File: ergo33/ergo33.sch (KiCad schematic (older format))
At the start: 113 parts, among them SW1 SW_Push, SW46 Rotary_Encoder_Switch, U1 ATmega32U4-AU, Y1 16MHz

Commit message: Start trace layout
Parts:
- removed F2: 500mA, Fuse:Fuse_1206_3216Metric, symbol Device:Polyfuse_Small
- added JP4: SolderJumper_2_Open, Jumper:SolderJumper-2_P1.3mm_Open_Pad1.0x1.5mm, symbol Jumper:SolderJumper_2_Open
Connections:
- net at USB2.5 (VBUS): now also JP4.1 (A)
- net PWR_IN: now reaches F1.1, USB1.16 (VBUS), USB1.21 (VBUS), USB1.4 (VBUS), USB1.9 (VBUS)
- net PWR_IN: now also JP4.2 (B)
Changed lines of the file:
@@
 	4400 6350 5000 6350
 Wire Wire Line
-	1650 6150 1900 6150
+	1650 6150 1850 6150
 Connection ~ 1650 6150
 $Comp
@@
 Text GLabel 2100 6450 2    50   Input ~ 0
 D-
-Wire Wire Line
-	2100 6150 2250 6150
-$Comp
-L Device:Polyfuse_Small F2
-U 1 1 5F2186AC
-P 2000 6150
-F 0 "F2" V 1795 6150 50  0000 C CNN
-F 1 "500mA" V 1886 6150 50  0000 C CNN
-F 2 "Fuse:Fuse_1206_3216Metric" H 2050 5950 50  0001 L CNN
-F 3 "~" H 2000 6150 50  0001 C CNN
-	1    2000 6150
-	0    1    1    0
-$EndComp
-$Comp
-L power:+5V #PWR0116
-U 1 1 5F210B55
-P 2250 6150
-F 0 "#PWR0116" H 2250 6000 50  0001 C CNN
-F 1 "+5V" H 2265 6323 50  0000 C CNN
-F 2 "" H 2250 6150 50  0001 C CNN
-F 3 "" H 2250 6150 50  0001 C CNN
-	1    2250 6150
-	1    0    0    -1
-$EndComp
 Connection ~ 1350 6550
 Wire Wire Line
@@
 Wire Wire Line
 	10900 5950 10950 5950
+$Comp
+L Jumper:SolderJumper_2_Open JP4
+U 1 1 5F1CFCA6
+P 2000 6150
+F 0 "JP4" H 2000 6355 50  0000 C CNN
+F 1 "SolderJumper_2_Open" H 2000 6264 50  0000 C CNN
+F 2 "Jumper:SolderJumper-2_P1.3mm_Open_Pad1.0x1.5mm" H 2000 6150 50  0001 C CNN
+F 3 "~" H 2000 6150 50  0001 C CNN
+	1    2000 6150
+	1    0    0    -1
+$EndComp
+Wire Wire Line
+	2150 6150 2250 6150
+Text GLabel 2250 6150 2    50   Input ~ 0
+PWR_IN
+Text GLabel 4850 5850 3    50   Input ~ 0
+PWR_IN
 $EndSCHEMATC

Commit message: Rerouting ergo33
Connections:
- net ROW0: now also U1.41 (PF0)
- net ROW1: now also U1.40 (PF1)
- net ROW2: now also U1.39 (PF4)
- net ROW3: now also U1.38 (PF5)
- net ROW4: now also U1.37 (PF6)
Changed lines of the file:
@@
 Text GLabel 4850 5850 3    50   Input ~ 0
 PWR_IN
+Text GLabel 3150 4100 2    50   Input ~ 0
+ROW0
+Text GLabel 3150 4200 2    50   Input ~ 0
+ROW1
+Text GLabel 3150 4300 2    50   Input ~ 0
+ROW2
+Text GLabel 3150 4400 2    50   Input ~ 0
+ROW3
+Text GLabel 3150 4500 2    50   Input ~ 0
+ROW4
 $EndSCHEMATC

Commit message: Finish ergo33 routing v1
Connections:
- net COL0: now also U1.32 (PC7)
- net COL1: now also U1.31 (PC6)
- net COL2: now also U1.30 (PB6)
- net COL3: now also U1.29 (PB5)
- net COL4: now also U1.28 (PB4)
- net COL5: now also U1.27 (PD7)
- net COL6: now also U1.26 (PD6)
- net LEDS: now also JP1.2 (C), U1.25 (PD4); no longer JP1.1 (A)
- net at LED1.4 (DIN): now also JP1.1 (A); no longer JP1.2 (C)
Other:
- moved on the sheet: JP1, R4
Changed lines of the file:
@@
 L Device:R_Small R4
 U 1 1 5F14E7F9
-P 3350 3800
-F 0 "R4" V 3154 3800 50  0000 C CNN
-F 1 "10k" V 3245 3800 50  0000 C CNN
-F 2 "Resistor_SMD:R_0805_2012Metric" H 3350 3800 50  0001 C CNN
-F 3 "~" H 3350 3800 50  0001 C CNN
-	1    3350 3800
+P 3450 3800
+F 0 "R4" V 3254 3800 50  0000 C CNN
+F 1 "10k" V 3345 3800 50  0000 C CNN
+F 2 "Resistor_SMD:R_0805_2012Metric" H 3450 3800 50  0001 C CNN
+F 3 "~" H 3450 3800 50  0001 C CNN
+	1    3450 3800
 	0    1    1    0
 $EndComp
@@
 	1    0    0    -1
 $EndComp
-Wire Wire Line
-	3150 3800 3250 3800
-Wire Wire Line
-	3450 3800 3600 3800
 $Comp
 L Device:R_Small R3
@@
 	1    0    0    -1
 $EndComp
-Text GLabel 5400 4450 0    50   Input ~ 0
+Text GLabel 5750 4450 2    50   Input ~ 0
 LEDS
 Wire Wire Line
@@
 	1300 2000 1200 2000
 Wire Wire Line
-	5600 4600 5600 4850
-Wire Wire Line
 	10800 6050 10800 5700
 Connection ~ 10800 6050
 Wire Wire Line
 	10800 6050 10950 6050
-Text GLabel 5800 4450 2    50   Input ~ 0
+Text GLabel 5600 4250 1    50   Input ~ 0
 LEDS2
 Wire Wire Line
@@
 F 3 "~" H 5600 4450 50  0001 C CNN
 	1    5600 4450
-	1    0    0    -1
+	0    -1   -1   0
 $EndComp
 Wire Wire Line
@@
 Text GLabel 3150 4500 2    50   Input ~ 0
 ROW4
+Wire Wire Line
+	5600 4650 5600 4850
+Text GLabel 3150 2700 2    50   Input ~ 0
+COL0
+Text GLabel 3150 2600 2    50   Input ~ 0
+COL1
+Text GLabel 3150 2300 2    50   Input ~ 0
+COL2
+Text GLabel 3150 2200 2    50   Input ~ 0
+COL3
+Text GLabel 3150 2100 2    50   Input ~ 0
+COL4
+Text GLabel 3150 3600 2    50   Input ~ 0
+COL5
+Wire Wire Line
+	3550 3800 3600 3800
+Wire Wire Line
+	3150 3800 3350 3800
+Text GLabel 3150 3500 2    50   Input ~ 0
+COL6
+Text GLabel 3150 3300 2    50   Input ~ 0
+LEDS
 $EndSCHEMATC

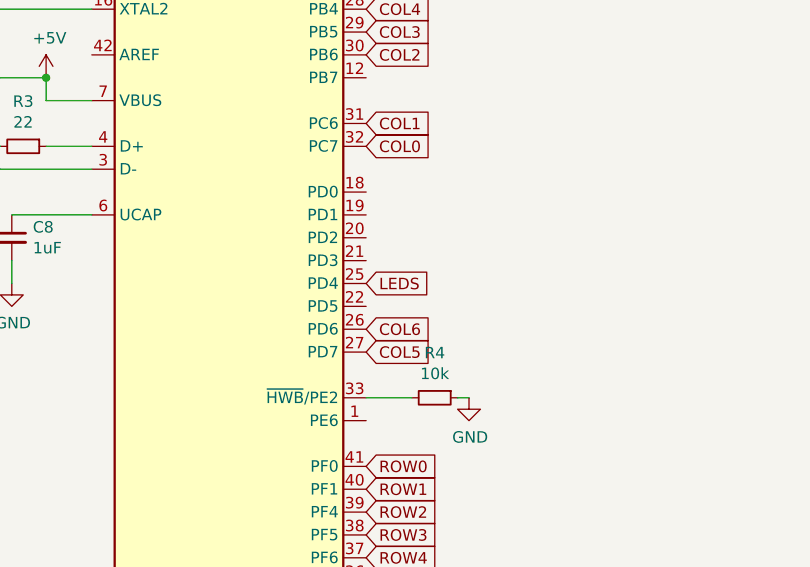
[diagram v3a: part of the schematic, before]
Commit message: Fix ergo33 routing
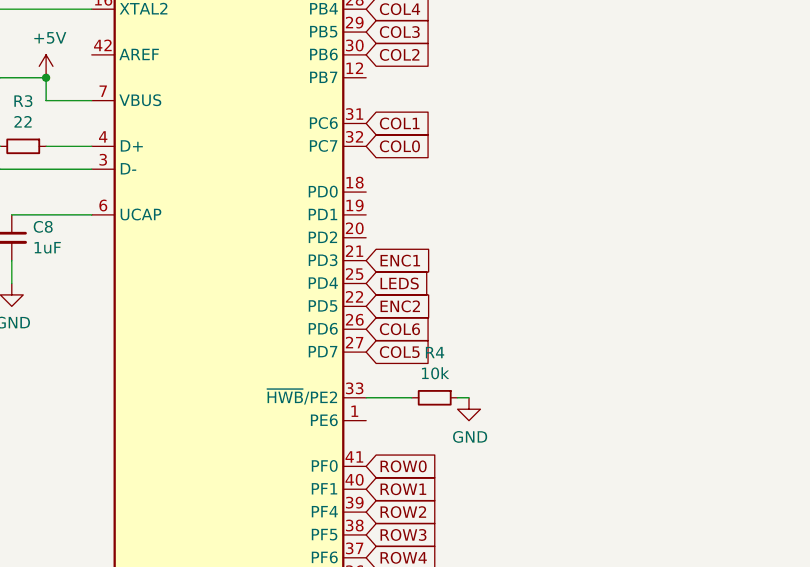
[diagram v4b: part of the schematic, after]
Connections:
- net ENC1: now also U1.21 (PD3)
- net ENC2: now also U1.22 (PD5)
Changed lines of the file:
@@
 Text GLabel 3150 3300 2    50   Input ~ 0
 LEDS
+Text GLabel 3150 3200 2    50   Input ~ 0
+ENC1
+Text GLabel 3150 3400 2    50   Input ~ 0
+ENC2
 $EndSCHEMATC

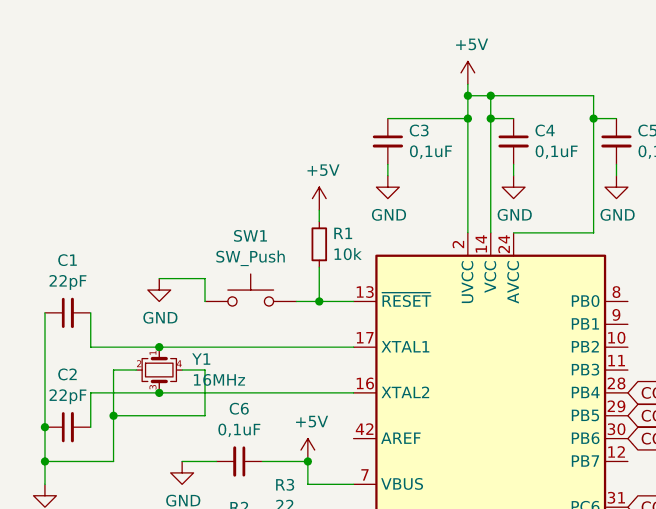
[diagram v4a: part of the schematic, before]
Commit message: Add arc suppression cap to ergo33
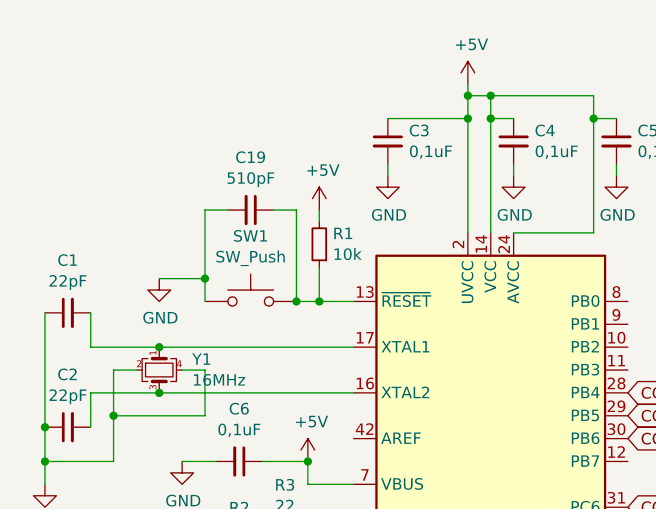
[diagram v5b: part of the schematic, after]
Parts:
- added C19: 510pF, Capacitor_SMD:C_0805_2012Metric, symbol Device:C_Small
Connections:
- net GND: now also C19.2
- net at R1.1, SW1.2, U1.13 (~RESET): now also C19.1
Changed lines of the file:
@@
 Text GLabel 3150 3400 2    50   Input ~ 0
 ENC2
+$Comp
+L Device:C_Small C19
+U 1 1 5F1BC5FF
+P 1500 1300
+F 0 "C19" V 1271 1300 50  0000 C CNN
+F 1 "510pF" V 1362 1300 50  0000 C CNN
+F 2 "Capacitor_SMD:C_0805_2012Metric" H 1500 1300 50  0001 C CNN
+F 3 "~" H 1500 1300 50  0001 C CNN
+	1    1500 1300
+	0    1    1    0
+$EndComp
+Wire Wire Line
+	1700 1700 1700 1300
+Wire Wire Line
+	1700 1300 1600 1300
+Connection ~ 1700 1700
+Wire Wire Line
+	1400 1300 1300 1300
+Wire Wire Line
+	1300 1300 1300 1600
+Connection ~ 1300 1600
 $EndSCHEMATC

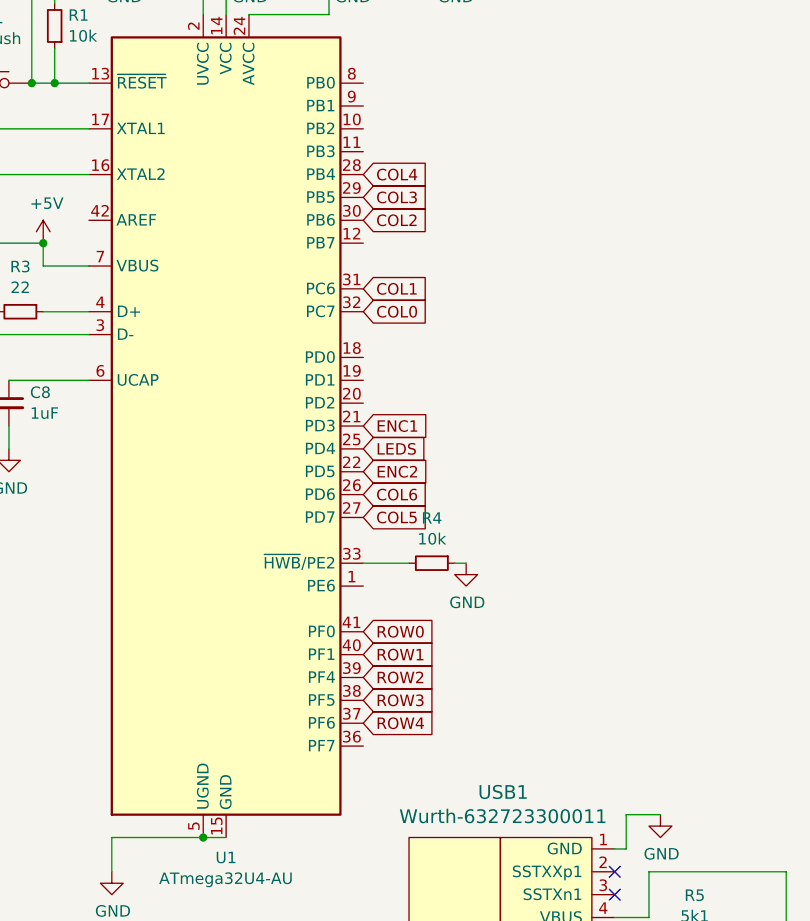
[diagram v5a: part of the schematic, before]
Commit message: Reroute ergo33 MCU area
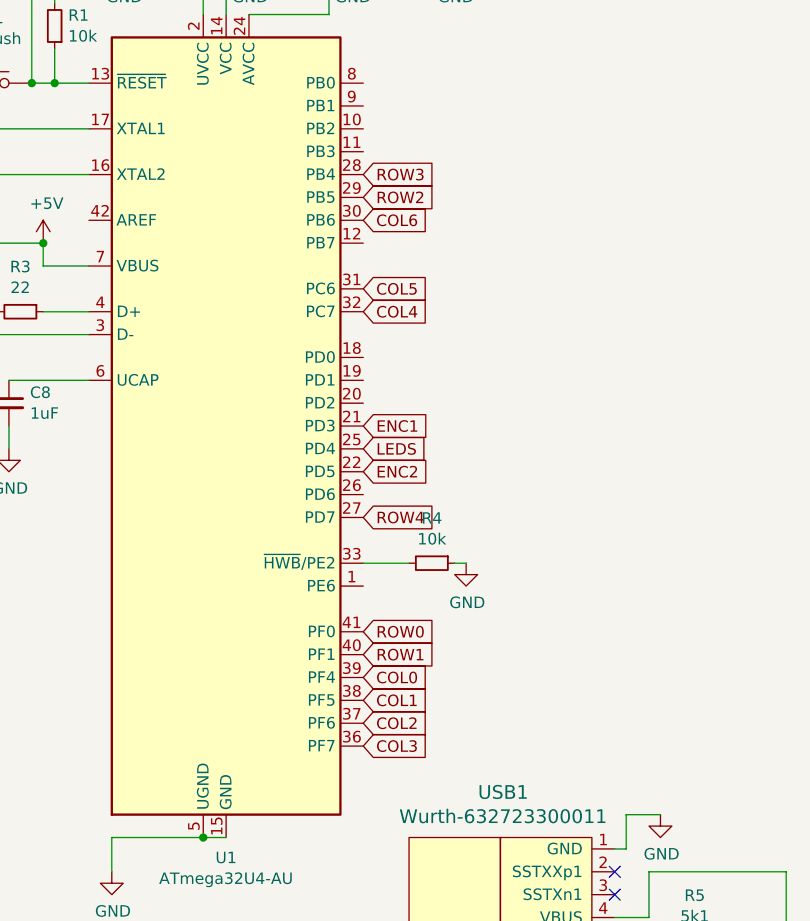
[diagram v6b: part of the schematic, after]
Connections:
- net COL0: now also U1.39 (PF4); no longer U1.32 (PC7)
- net COL1: now also U1.38 (PF5); no longer U1.31 (PC6)
- net COL2: now also U1.37 (PF6); no longer U1.30 (PB6)
- net COL3: now also U1.36 (PF7); no longer U1.29 (PB5)
- net COL4: now also U1.32 (PC7); no longer U1.28 (PB4)
- net COL5: now also U1.31 (PC6); no longer U1.27 (PD7)
- net COL6: now also U1.30 (PB6); no longer U1.26 (PD6)
- net ROW2: now also U1.29 (PB5); no longer U1.39 (PF4)
- net ROW3: now also U1.28 (PB4); no longer U1.38 (PF5)
- net ROW4: now also U1.27 (PD7); no longer U1.37 (PF6)
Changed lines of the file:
@@
 Text GLabel 3150 4200 2    50   Input ~ 0
 ROW1
-Text GLabel 3150 4300 2    50   Input ~ 0
+Text GLabel 3150 2200 2    50   Input ~ 0
 ROW2
-Text GLabel 3150 4400 2    50   Input ~ 0
+Text GLabel 3150 2100 2    50   Input ~ 0
 ROW3
-Text GLabel 3150 4500 2    50   Input ~ 0
+Text GLabel 3150 3600 2    50   Input ~ 0
 ROW4
 Wire Wire Line
 	5600 4650 5600 4850
+Text GLabel 3150 4300 2    50   Input ~ 0
+COL0
+Text GLabel 3150 4400 2    50   Input ~ 0
+COL1
+Text GLabel 3150 4500 2    50   Input ~ 0
+COL2
+Text GLabel 3150 4600 2    50   Input ~ 0
+COL3
 Text GLabel 3150 2700 2    50   Input ~ 0
-COL0
+COL4
 Text GLabel 3150 2600 2    50   Input ~ 0
-COL1
-Text GLabel 3150 2300 2    50   Input ~ 0
-COL2
-Text GLabel 3150 2200 2    50   Input ~ 0
-COL3
-Text GLabel 3150 2100 2    50   Input ~ 0
-COL4
-Text GLabel 3150 3600 2    50   Input ~ 0
 COL5
 Wire Wire Line
@@
 Wire Wire Line
 	3150 3800 3350 3800
-Text GLabel 3150 3500 2    50   Input ~ 0
+Text GLabel 3150 2300 2    50   Input ~ 0
 COL6
 Text GLabel 3150 3300 2    50   Input ~ 0

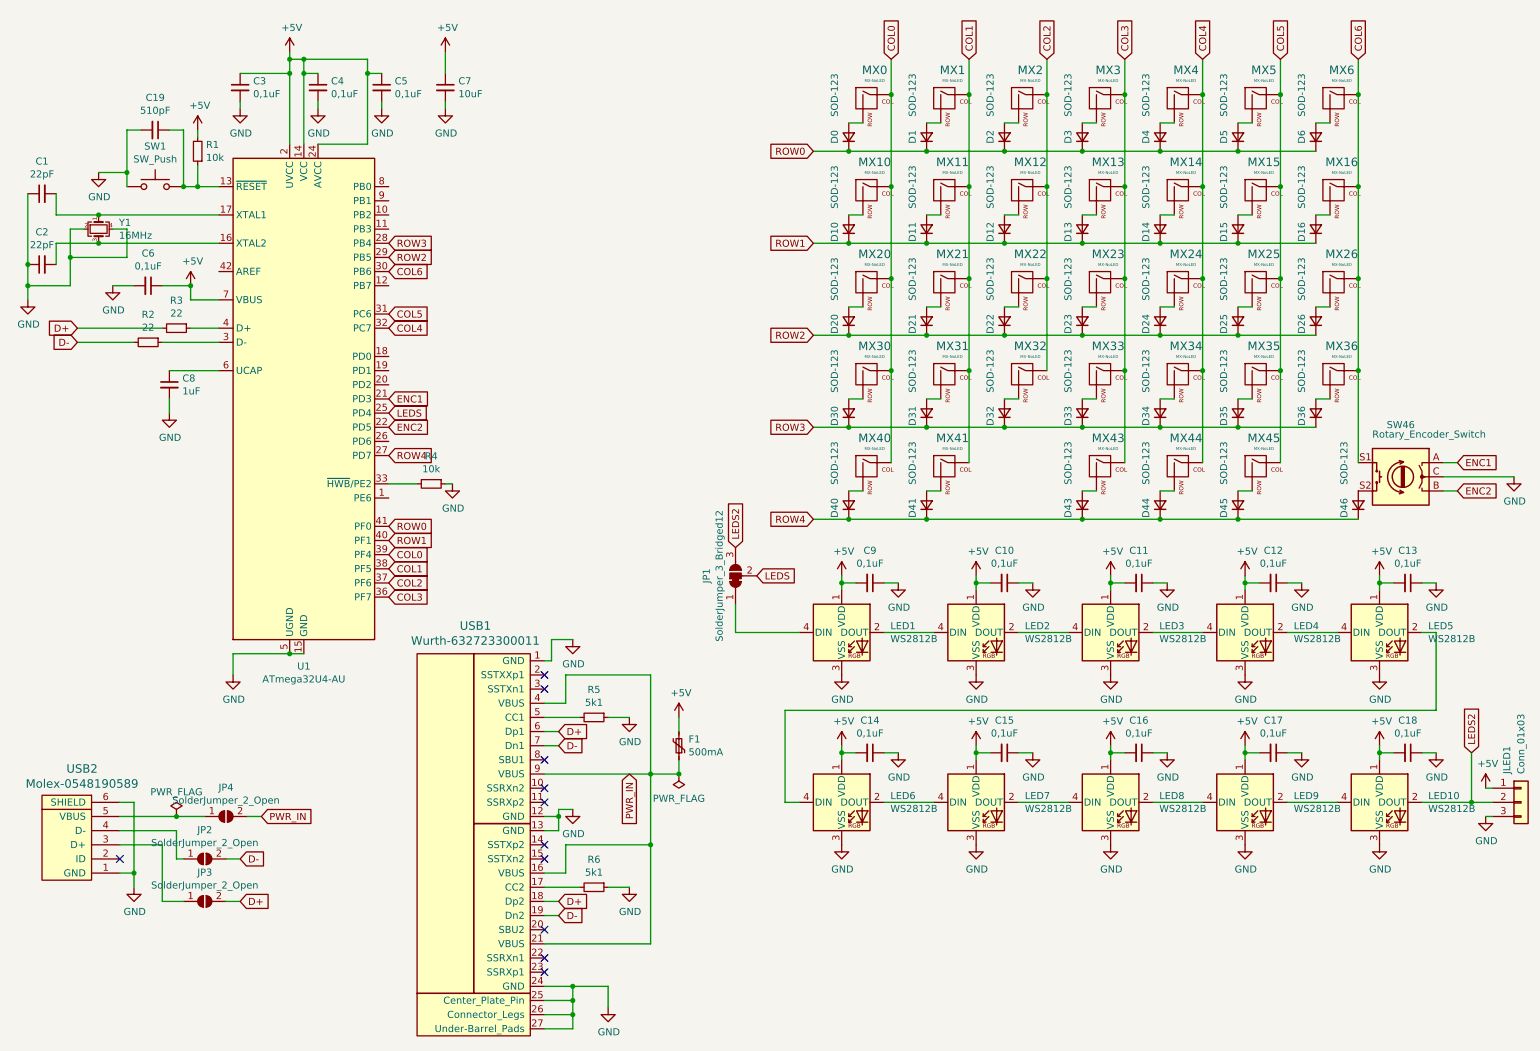
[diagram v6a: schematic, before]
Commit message: ergo33: Change USB connectors and add ESD protection
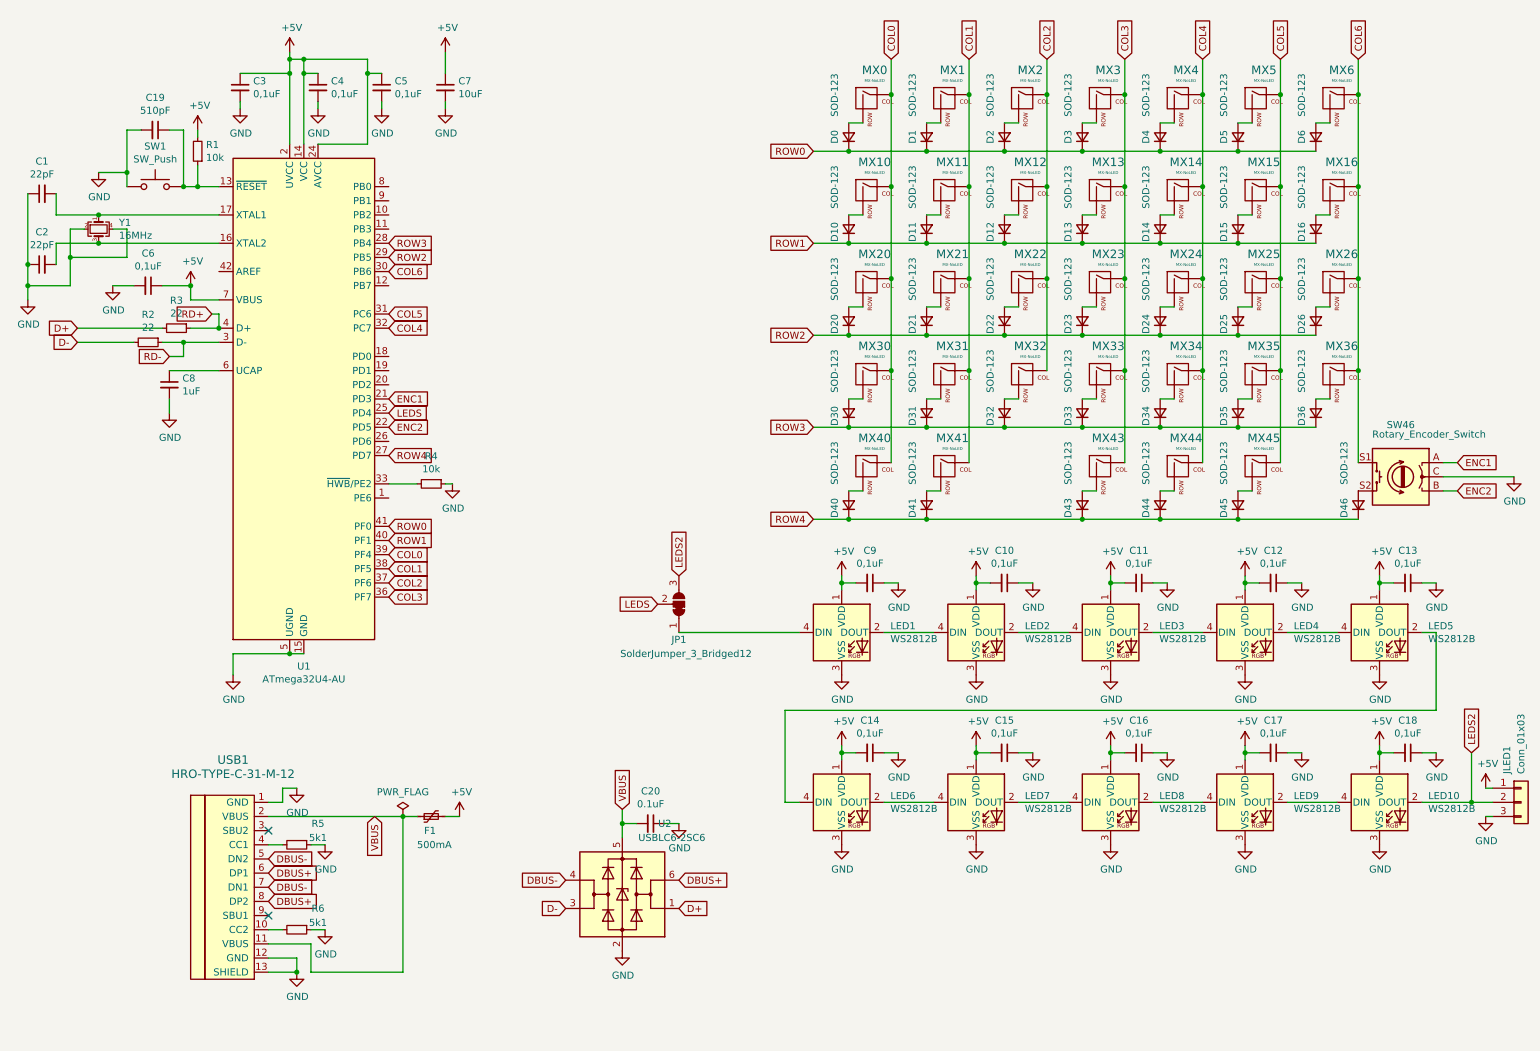
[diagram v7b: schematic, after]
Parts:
- removed JP2, JP3, JP4: SolderJumper_2_Open, Jumper:SolderJumper-2_P1.3mm_Open_Pad1.0x1.5mm, symbol Jumper:SolderJumper_2_Open
- removed USB1: Wurth-632723300011, Type-C:Wurth-632723300011-HandSoldering, symbol Type-C:Wurth-632723300011
- removed USB2: Molex-0548190589, random-keyboard-parts:Molex-0548190589, symbol random-keyboard-parts:Molex-0548190589
- added C20: 0.1uF, Capacitor_SMD:C_0805_2012Metric, symbol Device:C_Small
- added U2: USBLC6-2SC6, Package_TO_SOT_SMD:SOT-23-6_Handsoldering, symbol Power_Protection:USBLC6-2SC6
- added USB1: HRO-TYPE-C-31-M-12, Type-C:HRO-TYPE-C-31-M-12-HandSoldering, symbol Type-C:HRO-TYPE-C-31-M-12
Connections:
- net D+: now also U2.1 (I/O1)
- net D-: now also U2.3 (I/O2)
- net GND: now also C20.1, U2.2 (GND), USB1.1 (GND), USB1.12 (GND), USB1.13 (SHIELD)
- net RD-: now reaches R2.1, U1.3 (D-)
- net RD+: now reaches R3.1, U1.4 (D+)
- net at R6.2: now also USB1.10 (CC2)
- net at R5.2: now also USB1.4 (CC1)
- net PWR_IN renamed VBUS
- net VBUS: now also C20.2, U2.5 (VBUS), USB1.11 (VBUS), USB1.2 (VBUS)
- new net DBUS+: U2.6 (I/O1), USB1.6 (DP1), USB1.8 (DP2)
- new net DBUS-: U2.4 (I/O2), USB1.5 (DN2), USB1.7 (DN1)
- no-connect marks 11 -> 2
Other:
- moved on the sheet: JP1
